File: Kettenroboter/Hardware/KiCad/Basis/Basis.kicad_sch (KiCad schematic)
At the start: 69 parts, among them J1 Conn_01x03_Pin, J10 Screw_Terminal_01x02, J11 Conn_01x03, J12 Conn_01x03, J13 Conn_01x03, J14 Conn_01x03, J15 Conn_01x01, J16 Conn_01x03, J17 Conn_01x03, J2 Screw_Terminal_01x02, J21 Screw_Terminal_01x02, J22 Screw_Terminal_01x02, J23 Screw_Terminal_01x02, J24 Screw_Terminal_01x02, J3 Screw_Terminal_01x02, J4 Screw_Terminal_01x02, J5 Screw_Terminal_01x02, J6 Screw_Terminal_01x02, J7 Screw_Terminal_01x02, J8 Screw_Terminal_01x02, J9 Screw_Terminal_01x02, Q1 BSS138, Q2 BSS138, Q3 BSS138, Q4 BSS138, Q5 NMOS, Q6 NMOS, U2 NCP1117LPST33T3G, U3 SN74LS07

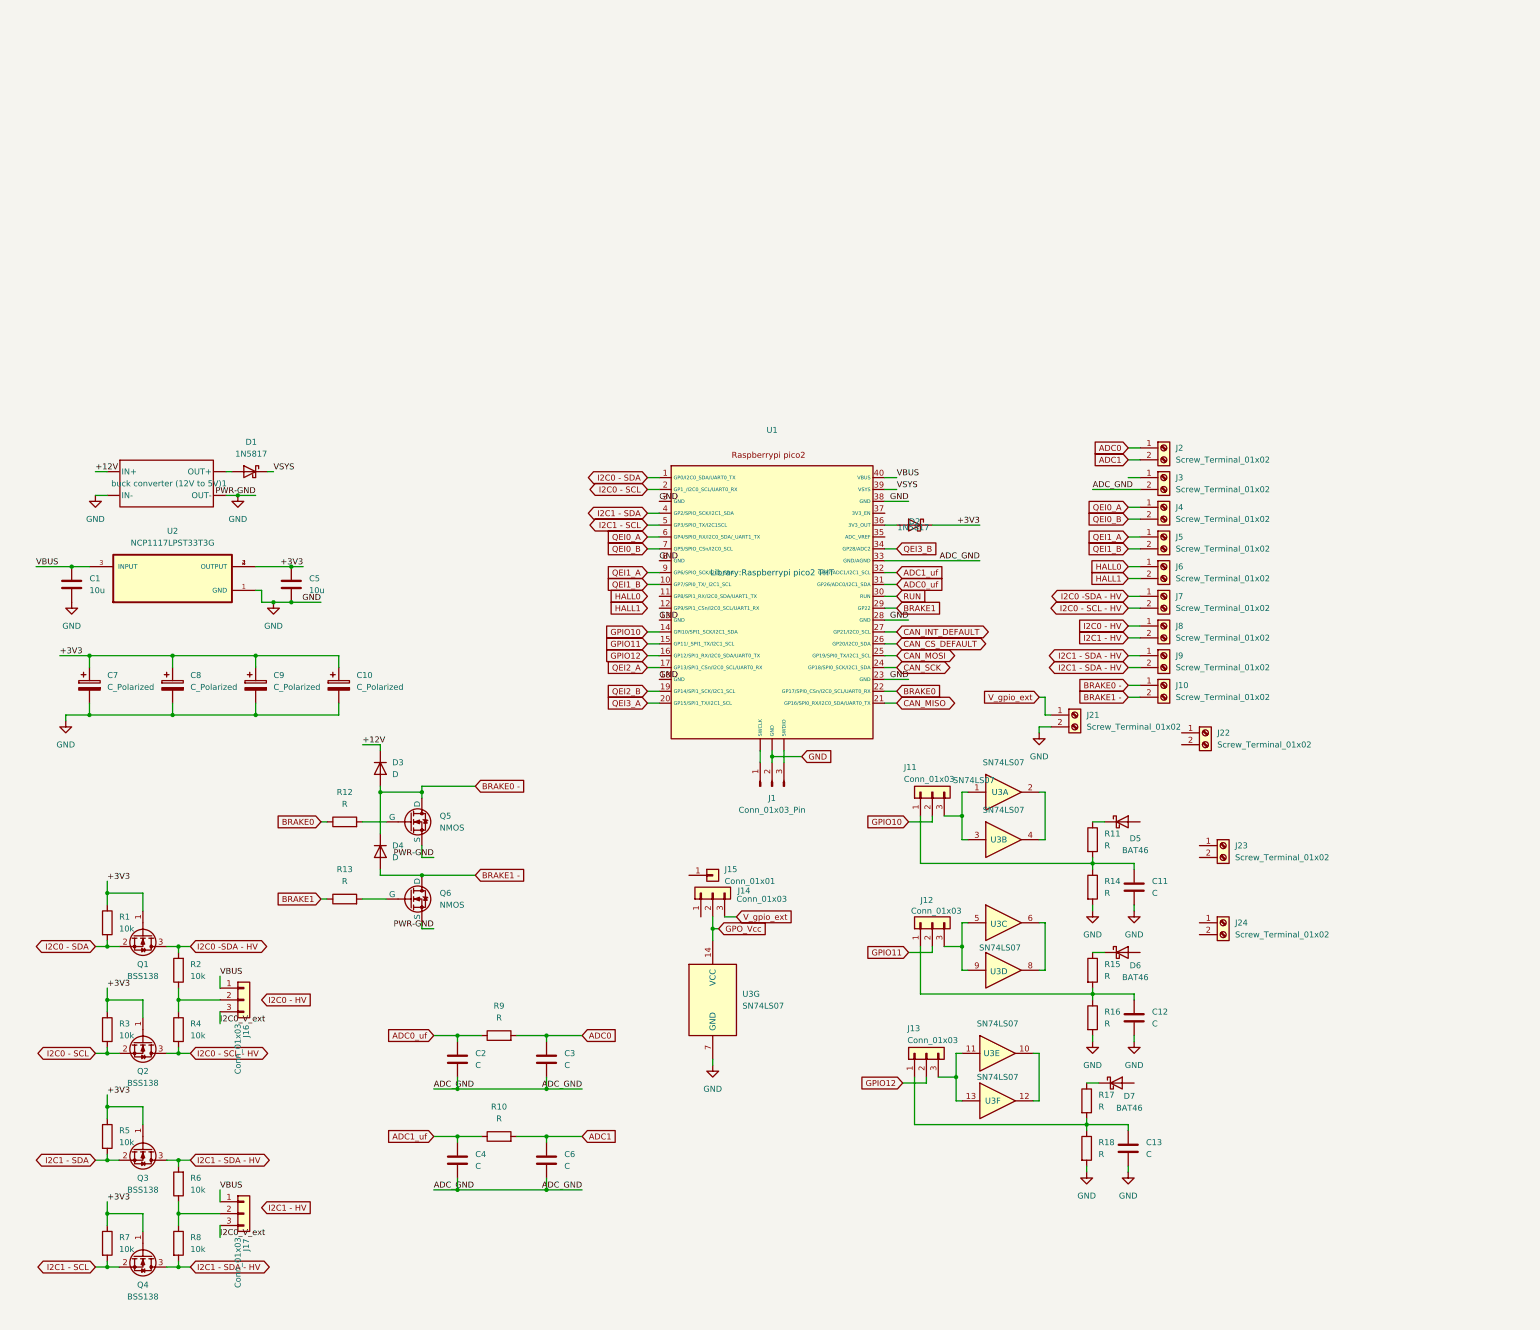
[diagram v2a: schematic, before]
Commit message: Neues Pico W Symol & Footprint
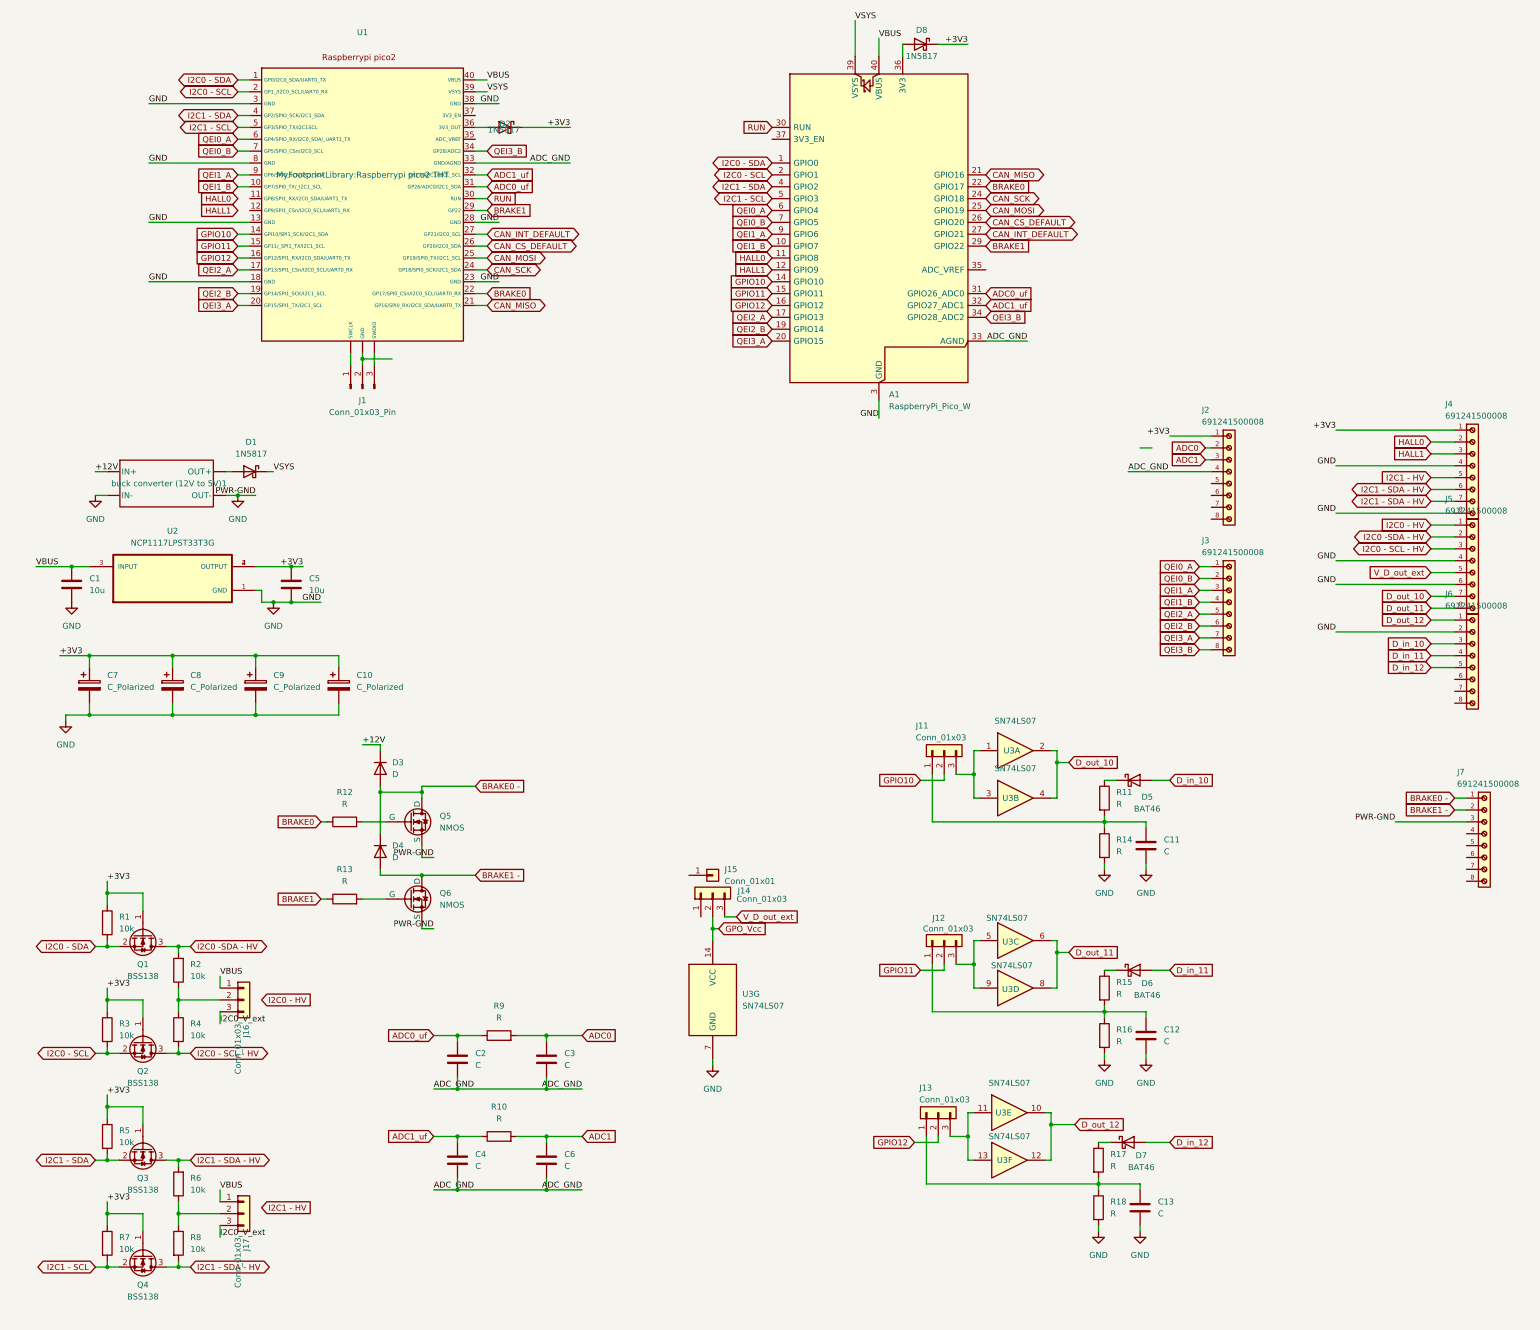
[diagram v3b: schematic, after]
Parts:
- removed J10, J2, J21, J22, J23, J24, J3, J4, J5, J6, J7, J8, J9: Screw_Terminal_01x02, Library:CONN_39773-0002_MOL, symbol Connector:Screw_Terminal_01x02
- removed U2: NCP1117LPST33T3G, NCP1117LPST33T3G:SOT230P700X175-4N, symbol Bachelorarbeit:NCP1117LPST33T3G
- added A1: RaspberryPi_Pico_W, Module:RaspberryPi_Pico_Common_THT, symbol MCU_Module:RaspberryPi_Pico_W
- added D8: 1N5817, Diode_THT:D_DO-41_SOD81_P10.16mm_Horizontal, symbol Diode:1N5817
- added J2, J3, J4, J5, J6, J7: 691241500008, Library:WR-TBL_V2_691241500008, symbol BA_screw_term2:691241500008
- added U2: NCP1117LPST33T3G, Library:NCP1117_SOT230P700X175-4N, symbol BA_NCP1117:NCP1117LPST33T3G
- U1: footprint Library:Raspberrypi pico2 THT -> MyFootprintLibrary:Raspberrypi pico2 THT
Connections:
- net +3V3: now also D8.1 (K), J2.1, J4.1, U2.2 (OUTPUT), U2.4 (OUTPUT)
- net ADC0: now also J2.2
- net ADC0_uf: now also A1.31 (GPIO26_ADC0)
- net ADC1: now also J2.3
- net ADC1_uf: now also A1.32 (GPIO27_ADC1)
- net ADC_GND: now also A1.33 (AGND), J2.4
- net BRAKE0: now also A1.22 (GPIO17)
- net BRAKE0 -: now also J7.1
- net BRAKE1: now also A1.29 (GPIO22)
- net BRAKE1 -: now also J7.2
- net CAN_CS_DEFAULT: now also A1.26 (GPIO20)
- net CAN_INT_DEFAULT: now also A1.27 (GPIO21)
- net CAN_MISO: now also A1.21 (GPIO16)
- net CAN_MOSI: now also A1.25 (GPIO19)
- net CAN_SCK: now also A1.24 (GPIO18)
- net GND: now also A1.13 (GND), A1.18 (GND), A1.23 (GND), A1.28 (GND), A1.3 (GND), A1.38 (GND), A1.8 (GND), J4.4, J4.8, J5.4, J5.6, J6.2, J7.3, U2.1 (GND); no longer J1.2 (Pin_2), U1. (SWDIO)
- net GPIO10: now also A1.14 (GPIO10)
- net GPIO11: now also A1.15 (GPIO11)
- net GPIO12: now also A1.16 (GPIO12)
- net HALL0: now also A1.11 (GPIO8), J4.2
- net HALL1: now also A1.12 (GPIO9), J4.3
- net I2C0 - HV: now also J5.1
- net I2C0 - SCL: now also A1.2 (GPIO1)
- net I2C0 - SCL - HV: now also J5.3
- net I2C0 - SDA: now also A1.1 (GPIO0)
- net I2C0 -SDA - HV: now also J5.2
- net I2C1 - HV: now also J4.5
- net I2C1 - SCL: now also A1.5 (GPIO3)
- net I2C1 - SDA: now also A1.4 (GPIO2)
- net I2C1 - SDA - HV: now also J4.6, J4.7
- net QEI0_A: now also A1.6 (GPIO4), J3.1
- net QEI0_B: now also A1.7 (GPIO5), J3.2
- net QEI1_A: now also A1.9 (GPIO6), J3.3
- net QEI1_B: now also A1.10 (GPIO7), J3.4
- net QEI2_A: now also A1.17 (GPIO13), J3.5
- net QEI2_B: now also A1.19 (GPIO14), J3.6
- net QEI3_A: now also A1.20 (GPIO15), J3.7
- net QEI3_B: now also A1.34 (GPIO28_ADC2), J3.8
- net RUN: now also A1.30 (RUN)
- net VBUS: now also A1.40 (VBUS), U2.3 (INPUT)
- net VSYS: now also A1.39 (VSYS)
- net D_out_11: now reaches U3.6, U3.8
- net D_out_11: now also J5.8
- net D_out_12: now reaches U3.10, U3.12
- net D_out_12: now also J6.1
- net D_out_10: now reaches U3.2, U3.4
- net D_out_10: now also J5.7
- net D_in_11: now reaches D6.2 (A)
- net D_in_11: now also J6.4
- net D_in_12: now reaches D7.2 (A)
- net D_in_12: now also J6.5
- net D_in_10: now reaches D5.2 (A)
- net D_in_10: now also J6.3
- net V_gpio_ext renamed V_D_out_ext
- net V_D_out_ext: now also J5.5
- new net: A1.36 (3V3), D8.2 (A)
- new net: J1.2 (Pin_2), U1. (SWDIO)
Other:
- moved on the sheet: C11, C12, C13, D2, D5, D6, D7, J1, J11, J12, J13, R11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

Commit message: pcb layout fnished
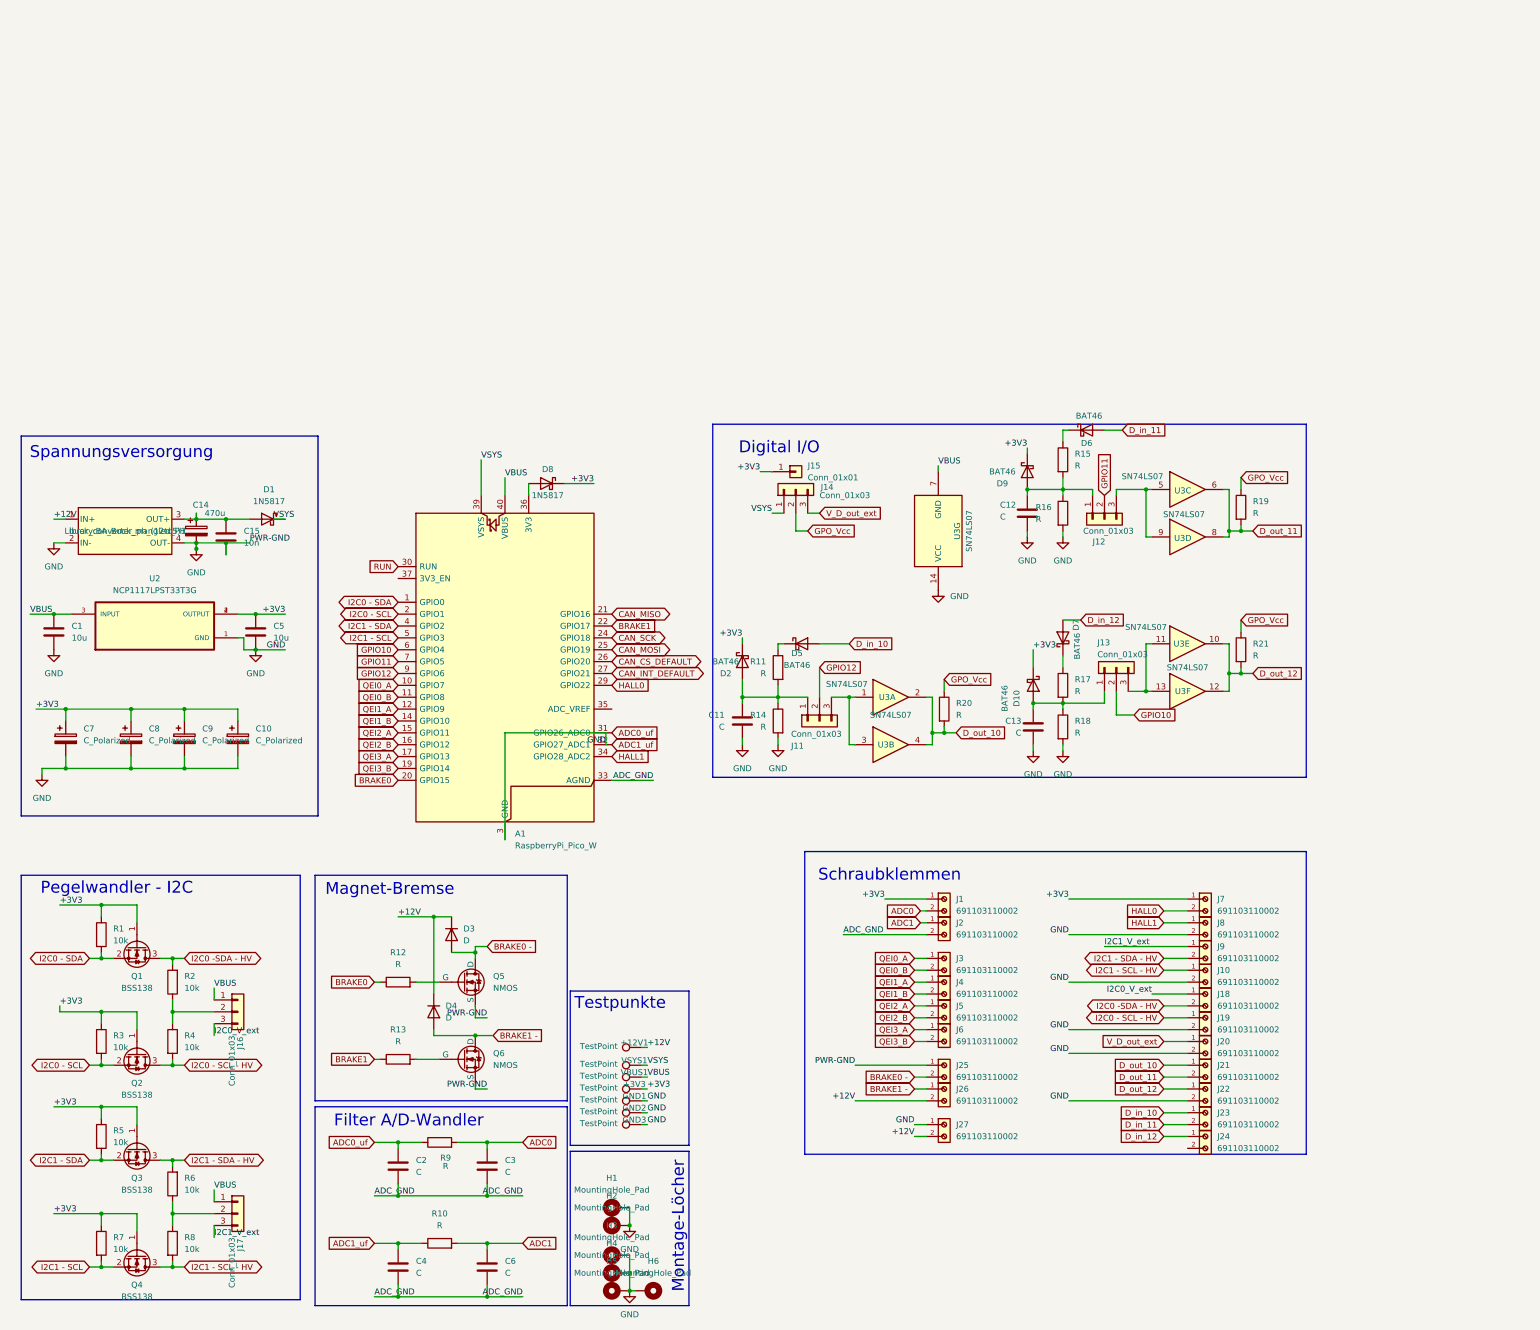
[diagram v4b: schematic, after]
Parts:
- removed D2: 1N5817, Diode_THT:D_DO-41_SOD81_P10.16mm_Horizontal, symbol Diode:1N5817
- removed J1: Conn_01x03_Pin, symbol Connector:Conn_01x03_Pin
- removed J2, J3, J4, J5, J6, J7: 691241500008, Library:WR-TBL_V2_691241500008, symbol BA_screw_term2:691241500008
- removed U1: ~, MyFootprintLibrary:Raspberrypi pico2 THT, symbol BA_Pico_2_W:U
- added +12V1, +3V3, GND1, GND2, GND3, VBUS1, VSYS1: TestPoint, TestPoint:TestPoint_Pad_D2.5mm, symbol Connector:TestPoint
- added C14: 470u, Capacitor_THT:CP_Radial_D5.0mm_P2.50mm, symbol Device:C_Polarized
- added C15: 10n, Capacitor_SMD:C_1206_3216Metric_Pad1.33x1.80mm_HandSolder, symbol Device:C
- added D10, D2, D9: BAT46, Diode_THT:D_DO-35_SOD27_P7.62mm_Horizontal, symbol Diode:BAT46
- added H1, H2: MountingHole_Pad, MountingHole:MountingHole_3.2mm_M3_Pad_Via, symbol Mechanical:MountingHole_Pad
- added H3, H4, H5, H6: MountingHole_Pad, MountingHole:MountingHole_4.3mm_M4_Pad_Via, symbol Mechanical:MountingHole_Pad
- added J1, J10, J18, J19, J2, J20, J21, J22, J23, J24, J25, J26, J27, J3, J4, J5, J6, J7, J8, J9: 691103110002, Library:WR-TBL_V3_2pin_691103110002, symbol BA_screw_term3_2pin:691103110002
- added R19, R20, R21: R, Resistor_SMD:R_1206_3216Metric_Pad1.30x1.75mm_HandSolder, symbol Device:R
- C11, C12, C13: footprint (none) -> Capacitor_SMD:C_1206_3216Metric_Pad1.33x1.80mm_HandSolder
- D3, D4: footprint (none) -> Diode_THT:D_5KPW_P7.62mm_Vertical_AnodeUp
- J11, J12, J13, J14, J16, J17: footprint (none) -> Connector_PinHeader_2.54mm:PinHeader_1x03_P2.54mm_Vertical
- J15: footprint (none) -> Connector_PinHeader_2.54mm:PinHeader_1x01_P2.54mm_Vertical
- R11, R14, R15, R16, R17, R18: footprint (none) -> Resistor_SMD:R_1206_3216Metric_Pad1.30x1.75mm_HandSolder
- buck_converter_ph_(12to5)1: renamed from buck converter (12V to 5V)1; footprint (none) -> Library:BA_Buck_mangled_PH
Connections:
- net +12V: now also D4.1 (K), buck_converter_ph_(12to5)1.1 (IN+), +12V1.1, J26.2, J27.2; no longer buck_converter_ph_(12to5)1. (OUT-)
- net +3V3: now also J15.1 (Pin_1), +3V3.1, D10.1 (K), D2.1 (K), D9.1 (K), J1.1, J7.1
- net ADC0: now also J1.2
- net ADC1: now also J2.1
- net ADC_GND: now also J2.2
- net BRAKE0: now also A1.20 (GPIO15); no longer A1.22 (GPIO17)
- net BRAKE0 -: now also J25.2; no longer D4.1 (K)
- net BRAKE1: now also A1.22 (GPIO17); no longer A1.29 (GPIO22)
- net BRAKE1 -: now also J26.1
- net D_in_10: now also J23.1
- net D_in_11: now also J23.2
- net D_in_12: now also J24.1
- net D_out_10: now also J21.1, R20.2
- net D_out_11: now also J21.2, R19.2
- net D_out_12: now also J22.1, R21.2
- net GND: now also U3.14 (VCC), buck_converter_ph_(12to5)1.2 (IN-), buck_converter_ph_(12to5)1.4 (OUT-), C14.2, C15.2, GND1.1, GND2.1, GND3.1, H1.1, H2.1, H3.1, H4.1, H5.1, H6.1, J10.2, J19.2, J20.2, J22.2, J25.1, J27.1, J8.2; no longer U3.7 (GND), buck_converter_ph_(12to5)1. (OUT-)
- net GPIO10: now also A1.6 (GPIO4), J13.2 (Pin_2); no longer A1.14 (GPIO10), J11.2 (Pin_2)
- net GPIO11: now also A1.7 (GPIO5); no longer A1.15 (GPIO11)
- net GPIO12: now also A1.9 (GPIO6), J11.2 (Pin_2); no longer A1.16 (GPIO12), J13.2 (Pin_2)
- net GPO_Vcc: now also R19.1, R20.1, R21.1; no longer U3.14 (VCC)
- net HALL0: now also A1.29 (GPIO22), J7.2; no longer A1.11 (GPIO8)
- net HALL1: now also A1.34 (GPIO28_ADC2), J8.1; no longer A1.12 (GPIO9)
- net I2C0 - SCL - HV: now also J19.1
- net I2C0 -SDA - HV: now also J18.2
- net I2C0_V_ext: now also J18.1; no longer J17.3 (Pin_3)
- net I2C1 - SDA - HV: now also J9.2; no longer Q4.3 (D), R8.2
- net QEI0_A: now also A1.10 (GPIO7), J3.1; no longer A1.6 (GPIO4)
- net QEI0_B: now also A1.11 (GPIO8), J3.2; no longer A1.7 (GPIO5)
- net QEI1_A: now also A1.12 (GPIO9), J4.1; no longer A1.9 (GPIO6)
- net QEI1_B: now also A1.14 (GPIO10), J4.2; no longer A1.10 (GPIO7)
- net QEI2_A: now also A1.15 (GPIO11), J5.1; no longer A1.17 (GPIO13)
- net QEI2_B: now also A1.16 (GPIO12), J5.2; no longer A1.19 (GPIO14)
- net QEI3_A: now also A1.17 (GPIO13), J6.1; no longer A1.20 (GPIO15)
- net QEI3_B: now also A1.19 (GPIO14), J6.2; no longer A1.34 (GPIO28_ADC2)
- net VBUS: now also U3.7 (GND), VBUS1.1
- net VSYS: now also J14.1 (Pin_1), VSYS1.1
- net V_D_out_ext: now also J20.1
- net at C11.1, J11.1 (Pin_1), R11.2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: now also D2.2 (A)
- net at C13.1, J13.1 (Pin_1), R17.2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: now also D10.2 (A)
- net at C12.1, J12.1 (Pin_1), R15.2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: now also D9.2 (A)
- net at D1.2 (A): now also buck_converter_ph_(12to5)1.3 (OUT+), C14.1, C15.1; no longer buck_converter_ph_(12to5)1. (OUT-)
- new net I2C1 - SCL - HV: J10.1, Q4.3 (D), R8.2
- new net I2C1_V_ext: J17.3 (Pin_3), J9.1
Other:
- note added: "Digital I/O"
- note added: "Filter A/D-Wandler"
- note added: "Magnet-Bremse"
- note added: "Montage-Löcher"
- note added: "Pegelwandler - I2C"
- note added: "Schraubklemmen"
- note added: "Spannungsversorgung"
- note added: "Testpunkte"
- moved on the sheet: A1, C1, C10, C11, C12, C13, C2, C3, C4, C5, C6, C7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

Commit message: Fast finale Version
Nach Crash gefixt
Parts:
- added C16: 10n, Capacitor_SMD:C_1206_3216Metric_Pad1.33x1.80mm_HandSolder, symbol Device:C
- added J28: Conn_01x02, Connector_PinHeader_2.54mm:PinHeader_1x02_P2.54mm_Vertical, symbol Connector_Generic:Conn_01x02
- added R23, R25, R27, R29, R31, R33, R35, R37: R, Resistor_SMD:R_1206_3216Metric_Pad1.30x1.75mm_HandSolder, symbol Device:R
- C1, C5: footprint (none) -> Capacitor_SMD:C_1206_3216Metric_Pad1.33x1.80mm_HandSolder
- C10, C7, C8, C9: footprint (none) -> Capacitor_THT:CP_Radial_D5.0mm_P2.50mm
- C3, C6: now not fitted
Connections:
- net ADC_GND is gone; now on net GND: A1.33 (AGND), C2.2, C3.2, C4.2, C6.2, J2.2
- net GND: now also J20.1, U3.7 (GND), C16.2, J28.2 (Pin_2), R23.2, R25.2, R27.2, R29.2, R31.2, R33.2, R35.2, R37.2; no longer J20.2, J25.1, Q5.3 (S), Q6.3 (S), U3.14 (VCC)
- net GPIO10: now also J11.2 (Pin_2); no longer J13.2 (Pin_2)
- net GPIO12: now also J13.2 (Pin_2); no longer J11.2 (Pin_2)
- net I2C0 -SDA - HV: no longer J18.2
- net QEI0_A: now also R23.1
- net QEI0_B: now also R25.1
- net QEI1_A: now also R27.1
- net QEI1_B: now also R29.1
- net QEI2_A: now also R33.1
- net QEI2_B: now also R35.1
- net QEI3_A: now also R37.1
- net QEI3_B: now also R31.1
- net RUN: now also J28.1 (Pin_1)
- net VBUS: no longer J16.1 (Pin_1), J17.1 (Pin_1), U3.7 (GND)
- net VSYS: now also J16.1 (Pin_1), J17.1 (Pin_1), U3.14 (VCC), C16.1
- net V_D_out_ext: now also J20.2; no longer J20.1
- new net I2C0 - SDA - HV: J18.2
- new net PWR-GND: J25.1, Q5.3 (S), Q6.3 (S)
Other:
- moved on the sheet: +12V1, +3V3, A1, D8, GND1, GND2, GND3, U3G, VBUS1, VSYS1
